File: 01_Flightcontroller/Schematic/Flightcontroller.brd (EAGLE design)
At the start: 63.5 x 59.4 mm, 86 parts, among them IC1 FT232RL, IC2 MPU6000, IC3 BMP280, J1 2908-05WB-MG, U1 STM32F7X2RXT, U2 ATMEGA328P_TQFP, U3 LM3940IMPX-3.3/NOPB, U4 TXB0104, Y1 8MHz, Y2 16MHz

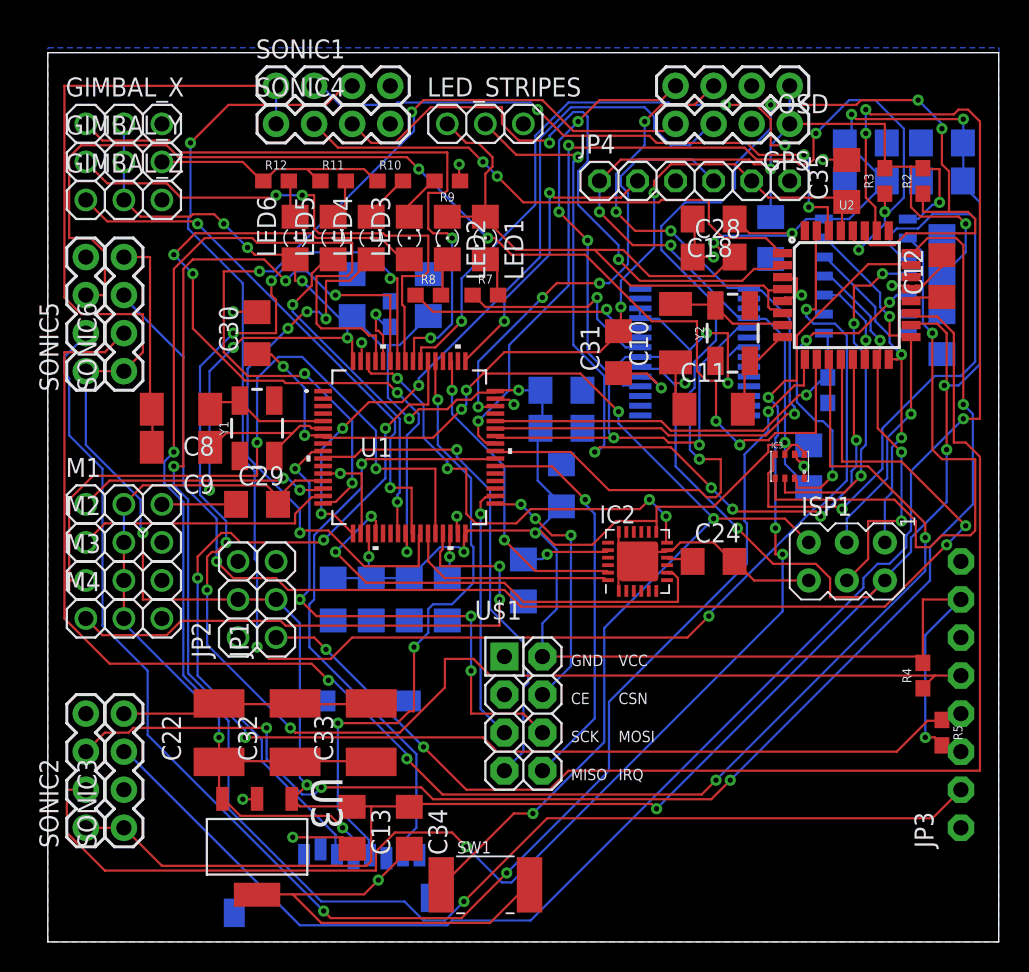
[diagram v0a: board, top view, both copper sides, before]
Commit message: Hinzufügen STNUCLEO144_MANUAL.pdf
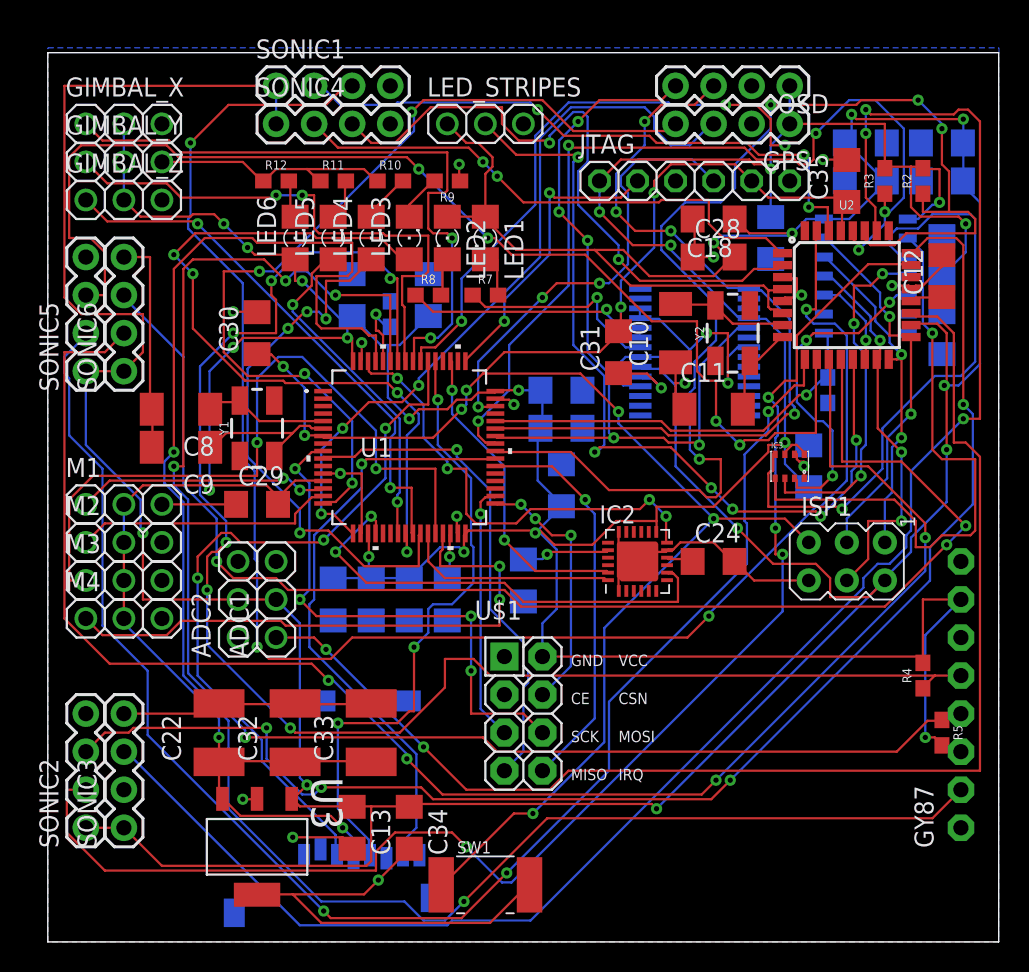
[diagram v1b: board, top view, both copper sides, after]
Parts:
- renumbered JP1 to ADC1, JP2 to ADC2, JP3 to GY87, JP4 to JTAG
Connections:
- removed net CS: U1.37
- net CE: now also U1.37
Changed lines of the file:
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@@
 <drawing>
 <settings>
-<setting alwaysvectorfont="yes"/>
+<setting alwaysvectorfont="no"/>
 <setting verticaltext="up"/>
 </settings>
@@
 <attribute name="VALUE" x="58.191390625" y="15.89111875" size="1.2702" layer="28" rot="MR270"/>
 </element>
-<element name="JP1" library="adafruit" library_urn="urn:adsk.eagle:library:420" package="1X03" package3d_urn="urn:adsk.eagle:package:6240710/1" value="" x="45.72" y="22.86" smashed="yes" rot="R90">
+<element name="ADC1" library="adafruit" library_urn="urn:adsk.eagle:library:420" package="1X03" package3d_urn="urn:adsk.eagle:package:6240710/1" value="" x="45.72" y="22.86" smashed="yes" rot="R90">
 <attribute name="NAME" x="43.8912" y="18.9738" size="1.27" layer="25" ratio="10" rot="R90"/>
 <attribute name="VALUE" x="48.895" y="19.05" size="1.27" layer="27" rot="R90"/>
 </element>
-<element name="JP2" library="adafruit" library_urn="urn:adsk.eagle:library:420" package="1X03" package3d_urn="urn:adsk.eagle:package:6240710/1" value="" x="43.18" y="22.86" smashed="yes" rot="R90">
+<element name="ADC2" library="adafruit" library_urn="urn:adsk.eagle:library:420" package="1X03" package3d_urn="urn:adsk.eagle:package:6240710/1" value="" x="43.18" y="22.86" smashed="yes" rot="R90">
 <attribute name="NAME" x="41.3512" y="18.9738" size="1.27" layer="25" ratio="10" rot="R90"/>
 <attribute name="VALUE" x="46.355" y="19.05" size="1.27" layer="27" rot="R90"/>
 </element>
-<element name="JP3" library="adafruit" library_urn="urn:adsk.eagle:library:420" package="1X08-CLEANBIG" package3d_urn="urn:adsk.eagle:package:6240708/1" value="" x="91.44" y="16.51" smashed="yes" rot="R90">
+<element name="GY87" library="adafruit" library_urn="urn:adsk.eagle:library:420" package="1X08-CLEANBIG" package3d_urn="urn:adsk.eagle:package:6240708/1" value="" x="91.44" y="16.51" smashed="yes" rot="R90">
 <attribute name="NAME" x="89.6112" y="6.2738" size="1.27" layer="25" ratio="10" rot="R90"/>
 <attribute name="VALUE" x="94.615" y="6.35" size="1.27" layer="27" rot="R90"/>
 </element>
-<element name="JP4" library="adafruit" library_urn="urn:adsk.eagle:library:420" package="1X06" package3d_urn="urn:adsk.eagle:package:6240711/1" value="" x="73.66" y="50.8" smashed="yes">
+<element name="JTAG" library="adafruit" library_urn="urn:adsk.eagle:library:420" package="1X06" package3d_urn="urn:adsk.eagle:package:6240711/1" value="" x="73.66" y="50.8" smashed="yes">
 <attribute name="NAME" x="65.9638" y="52.6288" size="1.27" layer="25" ratio="10"/>
 <attribute name="VALUE" x="66.04" y="47.625" size="1.27" layer="27"/>
@@
 <contactref element="SONIC5" pad="4"/>
 <contactref element="SONIC6" pad="4"/>
-<contactref element="JP1" pad="3"/>
-<contactref element="JP2" pad="3"/>
+<contactref element="ADC1" pad="3"/>
+<contactref element="ADC2" pad="3"/>
 <contactref element="GIMBAL_X" pad="3"/>
 <contactref element="GIMBAL_Z" pad="3"/>
 <contactref element="GIMBAL_Y" pad="3"/>
 <contactref element="GPS" pad="2"/>
-<contactref element="JP3" pad="6"/>
-<contactref element="JP4" pad="3"/>
+<contactref element="GY87" pad="6"/>
+<contactref element="JTAG" pad="3"/>
 <contactref element="ISP1" pad="6"/>
 <contactref element="R9" pad="1"/>
@@
 <contactref element="GIMBAL_Y" pad="2"/>
 <contactref element="GPS" pad="1"/>
-<contactref element="JP3" pad="7"/>
-<contactref element="JP4" pad="1"/>
+<contactref element="GY87" pad="7"/>
+<contactref element="JTAG" pad="1"/>
 <contactref element="LED6" pad="A"/>
 <contactref element="OSD" pad="1"/>
@@
 <contactref element="SONIC2" pad="1"/>
 <contactref element="SONIC1" pad="1"/>
-<contactref element="JP2" pad="2"/>
-<contactref element="JP1" pad="2"/>
+<contactref element="ADC2" pad="2"/>
+<contactref element="ADC1" pad="2"/>
 <contactref element="ISP1" pad="2"/>
 <contactref element="LED1" pad="A"/>
@@
 <signal name="SWDIO">
 <contactref element="U1" pad="46"/>
-<contactref element="JP4" pad="4"/>
+<contactref element="JTAG" pad="4"/>
 <wire x1="59.21375" y1="35.71875" x2="60.325" y2="35.71875" width="0.1524" layer="1"/>
 <wire x1="59.21375" y1="38.735" x2="59.21375" y2="35.71875" width="0.1524" layer="16"/>
@@
 <signal name="SWCLK">
 <contactref element="U1" pad="49"/>
-<contactref element="JP4" pad="2"/>
+<contactref element="JTAG" pad="2"/>
 <wire x1="60.96" y1="41.43375" x2="58.42" y2="38.89375" width="0.1524" layer="1"/>
 <wire x1="60.96" y1="42.8625" x2="60.96" y2="41.43375" width="0.1524" layer="16"/>
@@
 <signal name="SWO">
 <contactref element="U1" pad="55"/>
-<contactref element="JP4" pad="6"/>
+<contactref element="JTAG" pad="6"/>
 <wire x1="55.40375" y1="39.6875" x2="55.40375" y2="38.89375" width="0.1524" layer="1"/>
 <wire x1="56.35625" y1="39.6875" x2="55.40375" y2="39.6875" width="0.1524" layer="1"/>
@@
 <signal name="I2C1_SDA">
 <contactref element="U1" pad="59"/>
-<contactref element="JP3" pad="4"/>
+<contactref element="GY87" pad="4"/>
 <contactref element="R5" pad="1"/>
 <wire x1="90.4875" y1="15.24" x2="90.17" y2="14.9225" width="0.1524" layer="1"/>
@@
 <contactref element="U1" pad="58"/>
 <contactref element="R4" pad="1"/>
-<contactref element="JP3" pad="5"/>
+<contactref element="GY87" pad="5"/>
 <wire x1="89.69375" y1="17.78" x2="88.9" y2="16.98625" width="0.1524" layer="1"/>
 <wire x1="91.44" y1="17.78" x2="89.69375" y2="17.78" width="0.1524" layer="1"/>
@@
 <signal name="CE">
 <contactref element="U$1" pad="CE"/>
+<contactref element="U1" pad="37"/>
+<wire x1="60.96" y1="16.51" x2="60.36" y2="31.27" width="0" layer="19" extent="1-1"/>
 </signal>
 <signal name="I2C2_SCL">
@@
 <contactref element="C35" pad="1"/>
 <contactref element="C31" pad="2"/>
-<contactref element="JP4" pad="5"/>
+<contactref element="JTAG" pad="5"/>
 <contactref element="ISP1" pad="5"/>
 <contactref element="SW1" pad="P$1"/>
@@
 <signal name="ADC1">
 <contactref element="U2" pad="19"/>
-<contactref element="JP1" pad="1"/>
+<contactref element="ADC1" pad="1"/>
 <wire x1="88.42375" y1="41.75125" x2="88.265" y2="41.91" width="0.1524" layer="1"/>
 <wire x1="89.8525" y1="41.75125" x2="88.42375" y2="41.75125" width="0.1524" layer="1"/>
@@
 <signal name="ADC2">
 <contactref element="U2" pad="22"/>
-<contactref element="JP2" pad="1"/>
+<contactref element="ADC2" pad="1"/>
 <wire x1="43.18" y1="20.32" x2="88.1126" y2="44.38" width="0" layer="19" extent="1-1"/>
 </signal>
-<signal name="CS">
-<contactref element="U1" pad="37"/>
-</signal>
 <signal name="BATTSENS">
 <contactref element="U1" pad="22"/>
@@
 </signal>
 <signal name="FSYNC">
-<contactref element="JP3" pad="3"/>
+<contactref element="GY87" pad="3"/>
 </signal>
 <signal name="INTA">
-<contactref element="JP3" pad="2"/>
+<contactref element="GY87" pad="2"/>
 <contactref element="U1" pad="61"/>
 <wire x1="52.3875" y1="40.48125" x2="52.3875" y2="38.89375" width="0.1524" layer="1"/>
@@
 </signal>
 <signal name="DRDY">
-<contactref element="JP3" pad="1"/>
+<contactref element="GY87" pad="1"/>
 </signal>
 <signal name="N$13">

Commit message: JTAG -> Serial Wire
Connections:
- removed net JTDI: U1.50
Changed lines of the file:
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@@
 <via x="63.97625" y="50.00625" extent="1-16" drill="0.35"/>
-</signal>
-<signal name="JTDI">
-<contactref element="U1" pad="50"/>
 </signal>
 <signal name="SWO">
